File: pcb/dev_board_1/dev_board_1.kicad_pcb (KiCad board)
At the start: 2 copper layers, 90 x 97.5 mm, 89 parts, among them SW1 SW_DIP_x01, SW10 SW_DIP_x01, SW11 SW_DIP_x01, SW12 SW_DIP_x01, SW13 SW_DIP_x01, SW14 SW_DIP_x01, SW15 SW_DIP_x01, SW16 SW_DIP_x01, SW17 SW_DIP_x01, SW18 SW_DIP_x01, SW19 SW_DIP_x01, SW2 SW_DIP_x01, SW20 SW_DIP_x01, SW21 SW_DIP_x01, SW22 SW_DIP_x01, SW23 SW_DIP_x01, SW24 SW_DIP_x01, SW3 SW_DIP_x01, SW4 SW_DIP_x01, SW5 SW_DIP_x01, SW6 SW_DIP_x01, SW7 SW_DIP_x01, SW8 SW_DIP_x01, SW9 SW_DIP_x01, U2 LD3985M33R_SOT23, U3 STM32F427ZGTx, U4 MT48LC16M16A2TG, U6 STM32F427ZGTx, U7 MT48LC16M16A2TG

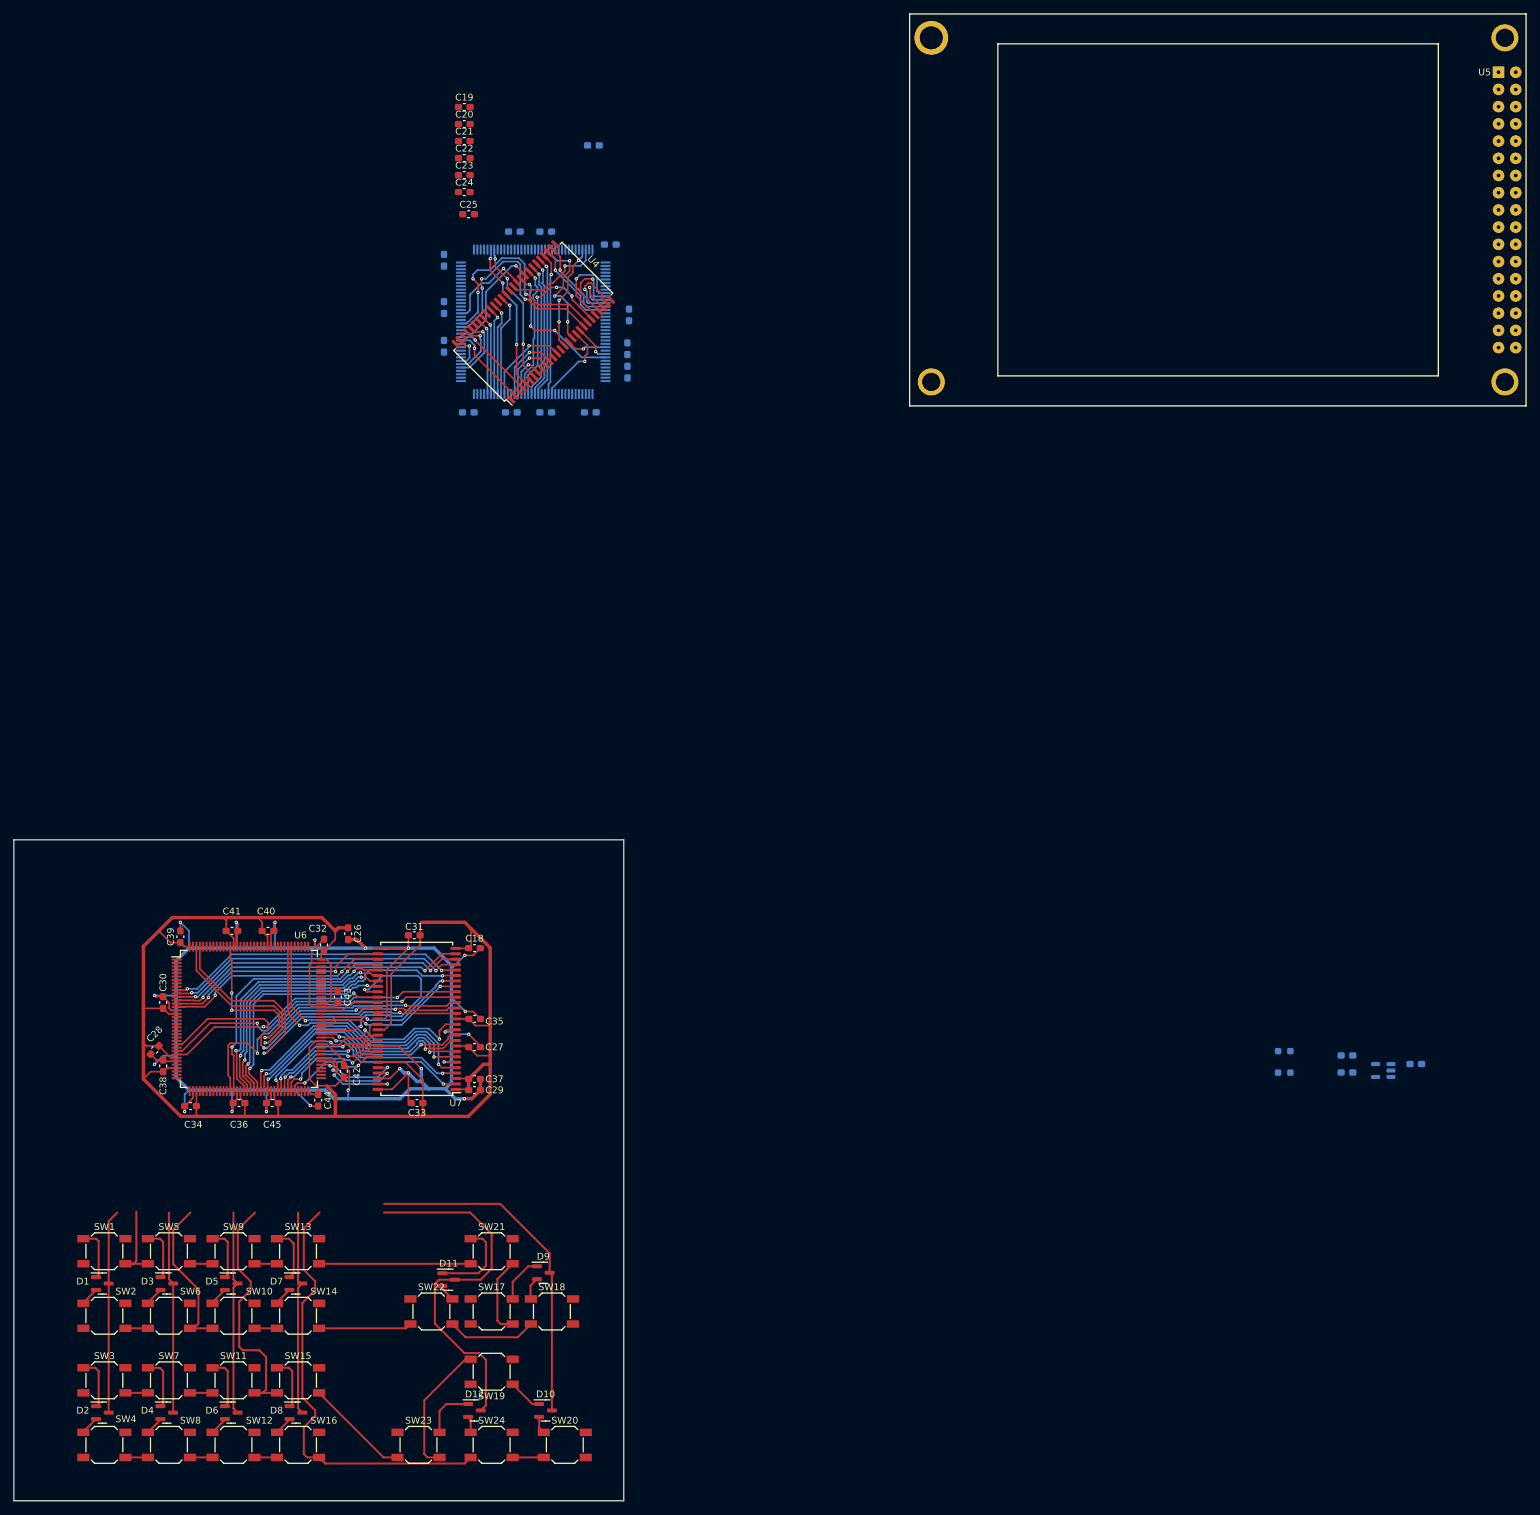
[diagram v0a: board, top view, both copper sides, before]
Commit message: add track to display and usb c
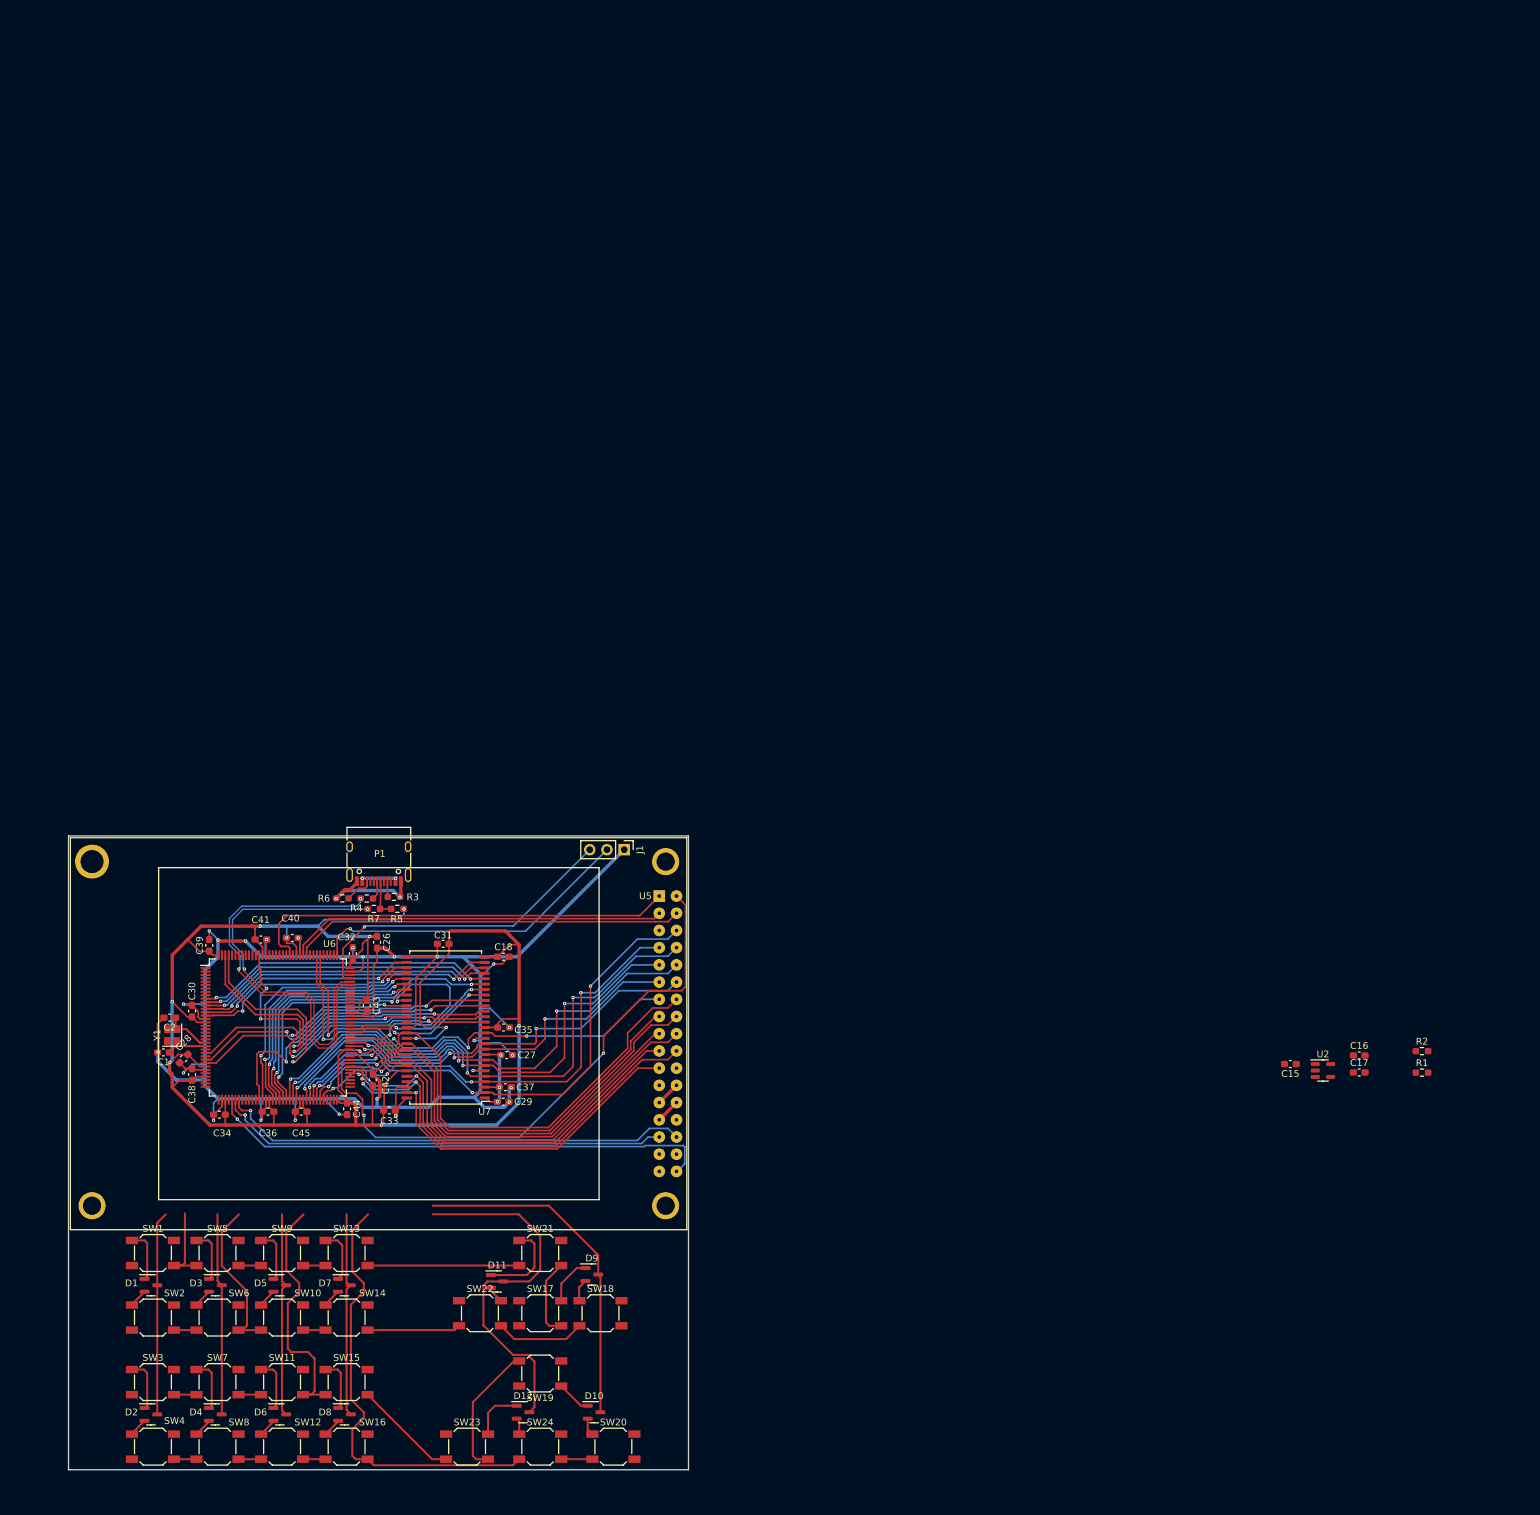
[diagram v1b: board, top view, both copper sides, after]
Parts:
- removed C10, C11, C12, C13, C14, C19, C20, C21, C22, C23, C24, C25, C3, C4, C5, C6, C7, C8, C9: 100nF, Capacitor_SMD:C_0603_1608Metric_Pad1.08x0.95mm_HandSolder
- removed U3: STM32F427ZGTx, Package_QFP:LQFP-144_20x20mm_P0.5mm
- removed U4: MT48LC16M16A2TG, Package_SO:TSOP-II-54_22.2x10.16mm_P0.8mm
- added J1: Conn_01x03, Connector_PinHeader_2.54mm:PinHeader_1x03_P2.54mm_Vertical, F.Cu at (117.9, 20.8)
- added P1: USB_C_Plug_USB2.0, Connector_USB:USB_C_Receptacle_HRO_TYPE-C-31-M-12, F.Cu at (81.7, 21.4)
- added R3: 5.1k, Resistor_SMD:R_0603_1608Metric_Pad0.98x0.95mm_HandSolder, F.Cu at (83.9, 27.7)
- added R4: 20R, Resistor_SMD:R_0603_1608Metric_Pad0.98x0.95mm_HandSolder, F.Cu at (79.9, 28.0)
- added R5: 1k, Resistor_SMD:R_0603_1608Metric_Pad0.98x0.95mm_HandSolder, F.Cu at (84.4, 29.5)
- added R6: 5.1k, Resistor_SMD:R_0603_1608Metric_Pad0.98x0.95mm_HandSolder, F.Cu at (76.3, 27.9)
- added R7: 20R, Resistor_SMD:R_0603_1608Metric_Pad0.98x0.95mm_HandSolder, F.Cu at (80.9, 29.5)
- added Y1: Crystal, Crystal:Crystal_SMD_2520-4Pin_2.5x2.0mm, F.Cu at (51.2, 48.1)
- C1: value 10mkF -> 20pF; moved to F.Cu
- C15, C16, C17, R1, R2, U2: moved to F.Cu
- C2: value 100nF -> 20pF; moved to F.Cu
- moved U5 173.5 mm to (127.0, 76.7)
- moved C1 148.1 mm to (49.9, 50.7), turned to 180 degrees
- moved C2 131.3 mm to (50.8, 45.5), turned to 180 degrees
- moved R1 20.3 mm to (235.6, 53.7), turned to 0 degrees
- moved R2 20.3 mm to (235.6, 50.5), turned to 0 degrees
- moved C15 18.5 mm to (216.2, 52.4), turned to 180 degrees
- moved U2 8.90 mm to (221.0, 53.3), turned to 0 degrees
- moved D10 7.17 mm to (113.4, 103.8)
- moved D7 7.17 mm to (76.6, 85.0)
- moved D8 7.17 mm to (76.6, 104.1)
- moved D9 7.17 mm to (113.1, 83.4)
- moved SW10 7.17 mm to (67.4, 89.8)
- moved SW11 7.17 mm to (67.4, 99.3)
- moved SW12 7.17 mm to (67.4, 108.8)
- moved SW17 7.17 mm to (105.5, 89.2)
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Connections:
- C1 pad 1: +3.3V -> osc2
- C2 pad 1: +3.3V -> osc1
- U6 pad 10: /TEST_1_FMC_A0 -> /FMC_A0
- U6 pad 103: unconnected-(U6-PA11-Pad103) -> USB_D-
- U6 pad 104: unconnected-(U6-PA12-Pad104) -> USB_D+
- U6 pad 105: unconnected-(U6-PA13-Pad105) -> SWDIO
- U6 pad 109: unconnected-(U6-PA14-Pad109) -> SWCLK
- U6 pad 11: /TEST_1_FMC_A1 -> /FMC_A1
- U6 pad 114: /TEST_1_FMC_D2 -> /FMC_D2
- U6 pad 115: /TEST_1_FMC_D3 -> /FMC_D3
- U6 pad 118: unconnected-(U6-PD4-Pad118) -> /FMC_NOE
- U6 pad 119: unconnected-(U6-PD5-Pad119) -> /FMC_NWE
- U6 pad 12: /TEST_1_FMC_A2 -> /FMC_A2
- U6 pad 123: unconnected-(U6-PD7-Pad123) -> /FMC_NE1
- U6 pad 13: /TEST_1_FMC_A3 -> /FMC_A3
- U6 pad 132: /TEST_1_FMC_~{CAS} -> /FMC_~{CAS}
- U6 pad 14: /TEST_1_FMC_A4 -> /FMC_A4
- U6 pad 141: /TEST_1_FMC_DQML -> /FMC_DQML
- U6 pad 142: /TEST_1_FMC_DQMH -> /FMC_DQMH
- U6 pad 15: /TEST_1_FMC_A5 -> /FMC_A5
- U6 pad 23: unconnected-(U6-PH0-Pad23) -> osc1
- U6 pad 24: unconnected-(U6-PH1-Pad24) -> osc2
- U6 pad 26: /TEST_1_FMC_~{WE} -> /FMC_~{WE}
- U6 pad 28: /TEST_1_FMC_~{CS} -> /FMC_~{CS}
- U6 pad 29: /TEST_1_FMC_CKE -> /FMC_CKE
- U6 pad 41: unconnected-(U6-PA5-Pad41) -> sck_touch
- U6 pad 42: unconnected-(U6-PA6-Pad42) -> miso_touch
- U6 pad 43: unconnected-(U6-PA7-Pad43) -> mosi_touch
- U6 pad 49: /TEST_1_FMC_~{RAS} -> /FMC_~{RAS}
- U6 pad 50: /TEST_1_FMC_A6 -> /FMC_A6
- U6 pad 53: /TEST_1_FMC_A7 -> /FMC_A7
- U6 pad 54: /TEST_1_FMC_A8 -> /FMC_A8
- U6 pad 55: /TEST_1_FMC_A9 -> /FMC_A9
- U6 pad 56: /TEST_1_FMC_A10 -> /FMC_A10
- U6 pad 57: /TEST_1_FMC_A11 -> /FMC_A11
- U6 pad 58: /TEST_1_FMC_D4 -> /FMC_D4
- U6 pad 59: /TEST_1_FMC_D5 -> /FMC_D5
- U6 pad 60: /TEST_1_FMC_D6 -> /FMC_D6
- U6 pad 63: /TEST_1_FMC_D7 -> /FMC_D7
- U6 pad 64: /TEST_1_FMC_D8 -> /FMC_D8
- U6 pad 65: /TEST_1_FMC_D9 -> /FMC_D9
- U6 pad 66: /TEST_1_FMC_D10 -> /FMC_D10
- U6 pad 67: /TEST_1_FMC_D11 -> /FMC_D11
- U6 pad 68: /TEST_1_FMC_D12 -> /FMC_D12
- U6 pad 77: /TEST_1_FMC_D13 -> /FMC_D13
- U6 pad 78: /TEST_1_FMC_D14 -> /FMC_D14
- U6 pad 79: /TEST_1_FMC_D15 -> /FMC_D15
- U6 pad 80: unconnected-(U6-PD11-Pad80) -> /FMC_A16
- U6 pad 85: /TEST_1_FMC_D0 -> /FMC_D0
- U6 pad 86: /TEST_1_FMC_D1 -> /FMC_D1
- U6 pad 87: /TEST_1_FMC_A12 -> /FMC_A12
- U6 pad 89: /TEST_1_FMC_BA0 -> /FMC_BA0
- U6 pad 90: /TEST_1_FMC_BA1 -> /FMC_BA1
- U6 pad 93: /TEST_1_FMC_CLK -> /FMC_CLK
- U7 pad 10: /TEST_1_FMC_D5 -> /FMC_D5
- U7 pad 11: /TEST_1_FMC_D6 -> /FMC_D6
- U7 pad 13: /TEST_1_FMC_D7 -> /FMC_D7
- U7 pad 15: /TEST_1_FMC_DQML -> /FMC_DQML
- U7 pad 16: /TEST_1_FMC_~{WE} -> /FMC_~{WE}
- U7 pad 17: /TEST_1_FMC_~{CAS} -> /FMC_~{CAS}
- U7 pad 18: /TEST_1_FMC_~{RAS} -> /FMC_~{RAS}
- U7 pad 19: /TEST_1_FMC_~{CS} -> /FMC_~{CS}
- U7 pad 2: /TEST_1_FMC_D0 -> /FMC_D0
- U7 pad 20: /TEST_1_FMC_BA0 -> /FMC_BA0
- U7 pad 21: /TEST_1_FMC_BA1 -> /FMC_BA1
- U7 pad 22: /TEST_1_FMC_A10 -> /FMC_A10
- U7 pad 23: /TEST_1_FMC_A0 -> /FMC_A0
- U7 pad 24: /TEST_1_FMC_A1 -> /FMC_A1
- U7 pad 25: /TEST_1_FMC_A2 -> /FMC_A2
- U7 pad 26: /TEST_1_FMC_A3 -> /FMC_A3
- U7 pad 29: /TEST_1_FMC_A4 -> /FMC_A4
- U7 pad 30: /TEST_1_FMC_A5 -> /FMC_A5
- U7 pad 31: /TEST_1_FMC_A6 -> /FMC_A6
- U7 pad 32: /TEST_1_FMC_A7 -> /FMC_A7
- U7 pad 33: /TEST_1_FMC_A8 -> /FMC_A8
- U7 pad 34: /TEST_1_FMC_A9 -> /FMC_A9
- U7 pad 35: /TEST_1_FMC_A11 -> /FMC_A11
- U7 pad 36: /TEST_1_FMC_A12 -> /FMC_A12
- U7 pad 37: /TEST_1_FMC_CKE -> /FMC_CKE
- U7 pad 38: /TEST_1_FMC_CLK -> /FMC_CLK
- U7 pad 39: /TEST_1_FMC_DQMH -> /FMC_DQMH
- U7 pad 4: /TEST_1_FMC_D1 -> /FMC_D1
- U7 pad 42: /TEST_1_FMC_D8 -> /FMC_D8
- U7 pad 44: /TEST_1_FMC_D9 -> /FMC_D9
- U7 pad 45: /TEST_1_FMC_D10 -> /FMC_D10
- U7 pad 47: /TEST_1_FMC_D11 -> /FMC_D11
- U7 pad 48: /TEST_1_FMC_D12 -> /FMC_D12
- U7 pad 5: /TEST_1_FMC_D2 -> /FMC_D2
- U7 pad 50: /TEST_1_FMC_D13 -> /FMC_D13
- U7 pad 51: /TEST_1_FMC_D14 -> /FMC_D14
- U7 pad 53: /TEST_1_FMC_D15 -> /FMC_D15
- U7 pad 7: /TEST_1_FMC_D3 -> /FMC_D3
- U7 pad 8: /TEST_1_FMC_D4 -> /FMC_D4
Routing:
- net /FMC_A16: track 0.00 -> 85.4 mm, vias 0 -> 2
- net sck_touch: track 0.00 -> 75.2 mm, vias 0 -> 1
- net /FMC_D4: track 6.61 -> 76.6 mm, vias 1 -> 3
- net mosi_touch: track 0.00 -> 69.7 mm, vias 0 -> 1
- net miso_touch: track 0.00 -> 66.9 mm, vias 0 -> 1
- net /FMC_D8: track 15.3 -> 80.4 mm, vias 1 -> 2
- net /FMC_NE1: track 0.00 -> 63.7 mm
- net USB_D-: track 0.00 -> 62.0 mm, vias 0 -> 2
- net /FMC_D2: track 22.1 -> 83.9 mm
- net /FMC_D10: track 13.2 -> 74.7 mm, vias 1 -> 2
- net USB_D+: track 0.00 -> 60.5 mm, vias 0 -> 2
- net /FMC_D5: track 8.80 -> 69.0 mm, vias 1 -> 3
- net /FMC_D9: track 13.8 -> 73.1 mm, vias 1 -> 2
- net /FMC_D12: track 11.3 -> 69.9 mm, vias 1 -> 2
- net /FMC_D6: track 10.5 -> 68.7 mm, vias 1 -> 3
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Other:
- board size 90 x 97.5 mm -> 91.5 x 93.5 mm

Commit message: place buttons
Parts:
- moved D11 0.45 mm to (99.4, 84.8)
- moved D12 0.45 mm to (103.3, 104.1)
- moved D5 0.45 mm to (67.4, 85.4)
- moved D6 0.45 mm to (67.4, 104.4)
- moved D1 0.45 mm to (48.4, 85.4)
- moved D2 0.45 mm to (48.4, 104.4)
- moved D3 0.45 mm to (57.9, 85.3)
- moved D4 0.45 mm to (57.8, 104.4)
- moved SW5 0.45 mm to (58.2, 80.6)
- moved SW6 0.45 mm to (58.2, 90.1)
- moved SW7 0.45 mm to (58.2, 99.6)
- moved SW8 0.45 mm to (58.2, 109.2)
- moved D10 0.45 mm to (113.8, 104.1)
- moved D7 0.45 mm to (76.9, 85.4)
- moved D8 0.45 mm to (76.9, 104.4)
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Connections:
- U6 pad 110: unconnected-(U6-PA15-Pad110) -> /LCD_RESET
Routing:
- net /LCD_RESET: track 0.00 -> 51.8 mm
- net +3.3V: track 310.1 -> 308.5 mm
